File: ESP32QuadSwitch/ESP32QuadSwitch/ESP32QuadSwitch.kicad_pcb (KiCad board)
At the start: 2 copper layers, 9 parts, among them J5 Conn_01x06_Pin, J6 B2+, J7 B1-, J8 B1+, J9 B2-, U1 ESP32-S2-WROVER

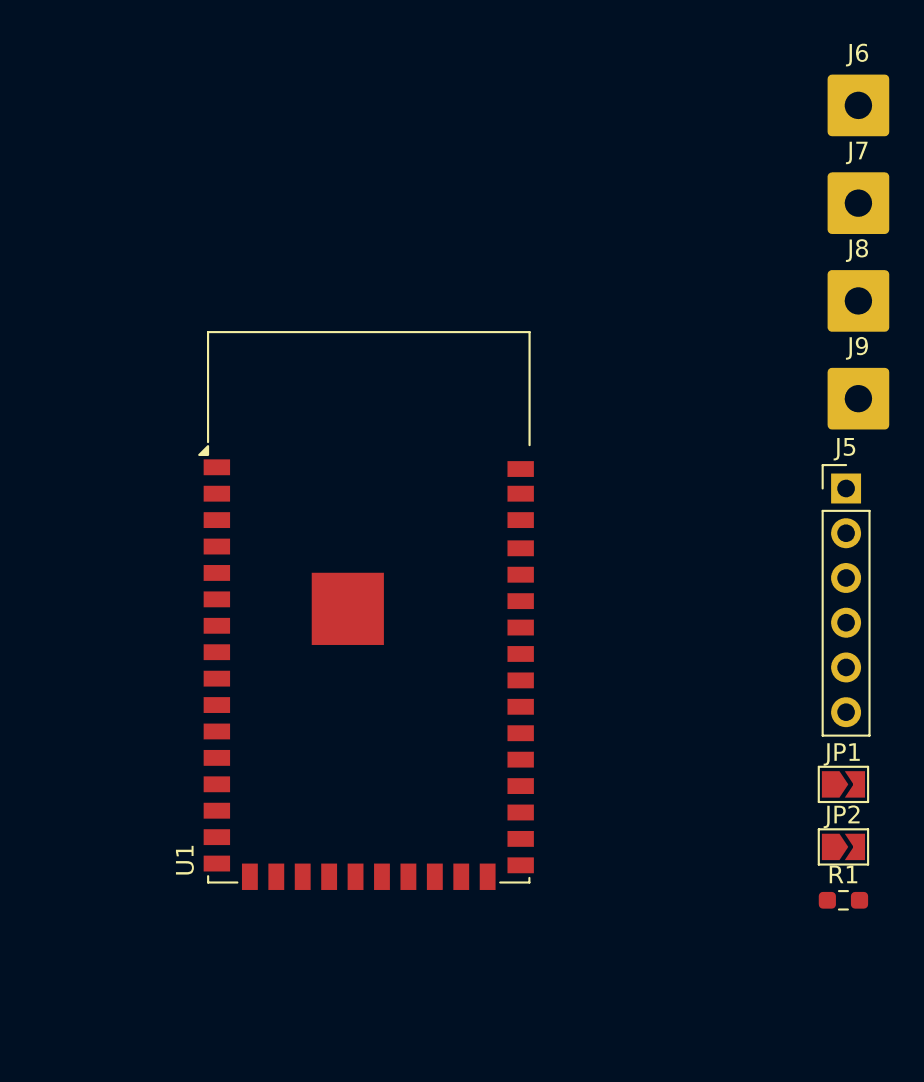
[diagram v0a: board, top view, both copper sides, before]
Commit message: new PCB with esp32-s2
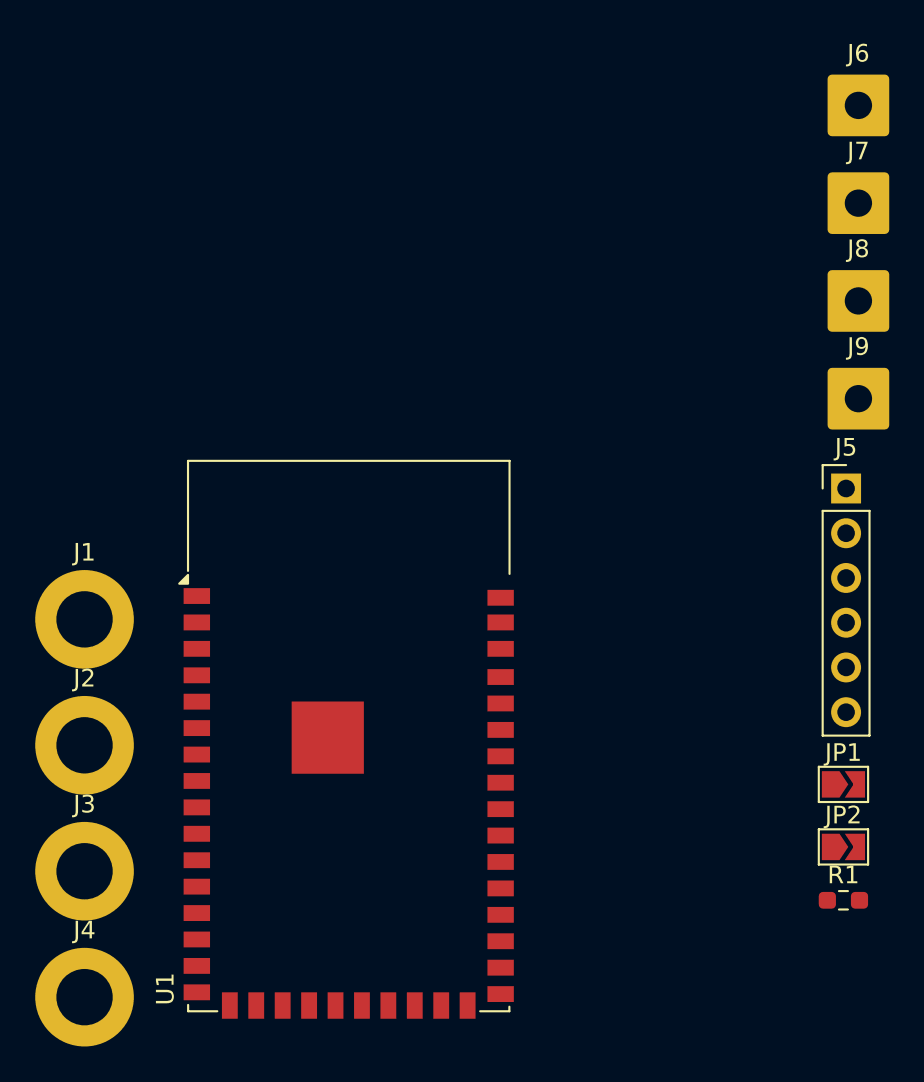
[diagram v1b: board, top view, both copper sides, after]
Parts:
- added J1: Conn_01x01_Pin, MountingHole:MountingHole_3.2mm_M3_DIN965_Pad, F.Cu at (100.0, 81.0)
- added J2: Conn_01x01_Pin, MountingHole:MountingHole_3.2mm_M3_DIN965_Pad, F.Cu at (100.0, 88.2)
- added J3: Conn_01x01_Pin, MountingHole:MountingHole_3.2mm_M3_DIN965_Pad, F.Cu at (100.0, 95.3)
- added J4: Conn_01x01_Pin, MountingHole:MountingHole_3.2mm_M3_DIN965_Pad, F.Cu at (100.0, 102.5)
- moved U1 7.40 mm to (115.0, 91.5)
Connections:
- JP2 pad 1: unconnected-(JP2-A-Pad1) -> Net-(J5-Pin_1)
